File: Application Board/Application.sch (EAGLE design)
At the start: 53 parts, among them Q1 DMP2012SN-7, T1 FDN340P, T2 AP1117_LIN_REG, U1 LM3409HV'LM3409HV'

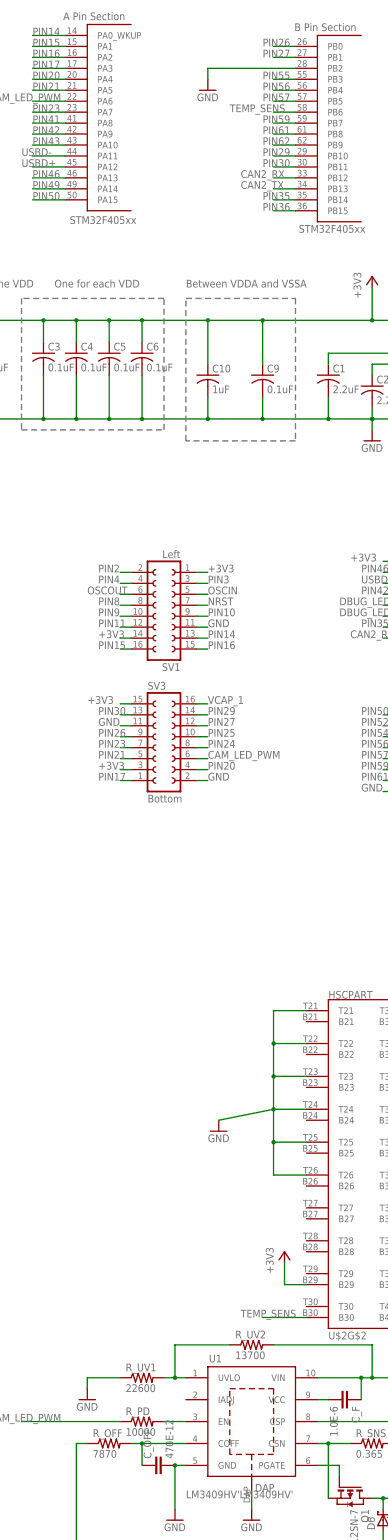
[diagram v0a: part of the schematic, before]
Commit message: Update 1/15/16 4:50pm
Added Temp_Sens Pullup Resistor, connected remaining air wires, modified
path of a few lines
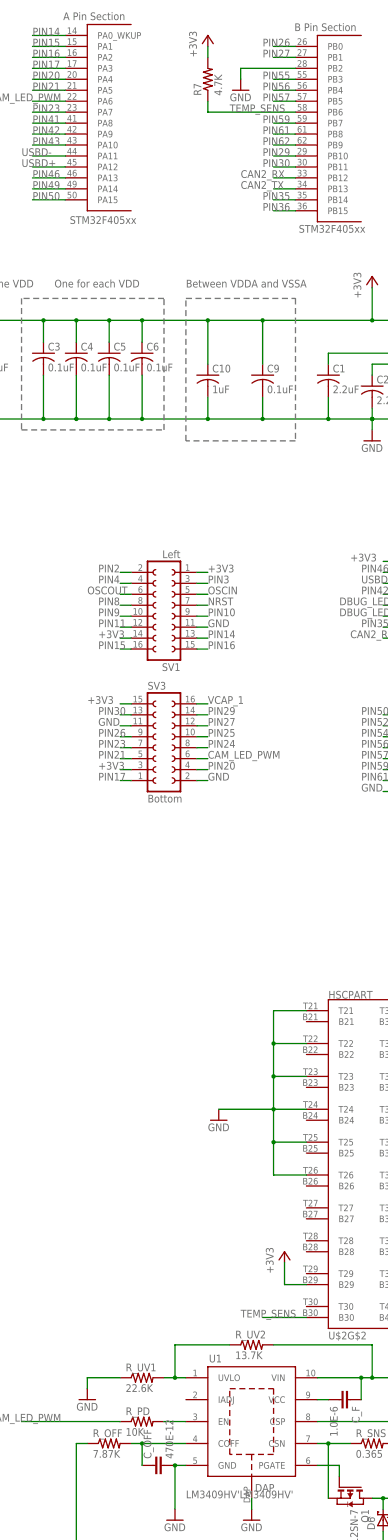
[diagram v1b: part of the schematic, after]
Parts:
- added R7: 4.7K, rcl:R-US_R0603
- R_OFF: value 7870 -> 7.87K
- R_PD: value 10000 -> 10K
- R_UV1: value 22600 -> 22.6K
- R_UV2: value 13700 -> 13.7K
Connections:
- net +3V3: now also R7.2
- net TEMP_SENS: now also R7.1
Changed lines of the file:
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@@
 <part name="+3V7" library="supply1" deviceset="+3V3" device=""/>
 <part name="GND11" library="supply1" deviceset="GND" device=""/>
-<part name="R_UV2" library="DiscreteComponents" deviceset="R-US_" device="R0603" value="13700"/>
-<part name="R_UV1" library="DiscreteComponents" deviceset="R-US_" device="R0603" value="22600"/>
-<part name="R_OFF" library="DiscreteComponents" deviceset="R-US_" device="R0603" value="7870"/>
+<part name="R_UV2" library="DiscreteComponents" deviceset="R-US_" device="R0603" value="13.7K"/>
+<part name="R_UV1" library="DiscreteComponents" deviceset="R-US_" device="R0603" value="22.6K"/>
+<part name="R_OFF" library="DiscreteComponents" deviceset="R-US_" device="R0603" value="7.87K"/>
 <part name="R_SNS" library="DiscreteComponents" deviceset="R-US_" device="R2512" value="0.365"/>
-<part name="R_PD" library="DiscreteComponents" deviceset="R-US_" device="R0603" value="10000"/>
+<part name="R_PD" library="DiscreteComponents" deviceset="R-US_" device="R0603" value="10K"/>
 <part name="L1" library="DiscreteComponents" deviceset="SRN8040" device="" value="15E-6"/>
 <part name="D6" library="DiscreteComponents" deviceset="SL12-E3/61T" device=""/>
@@
 <part name="P+5" library="supply1" deviceset="+12V" device=""/>
 <part name="GND18" library="supply1" deviceset="GND" device=""/>
+<part name="R7" library="rcl" deviceset="R-US_" device="R0603" value="4.7K"/>
+<part name="+3V5" library="supply1" deviceset="+3V3" device=""/>
 </parts>
 <sheets>
@@
 <instance part="+3V3" gate="G$1" x="198.12" y="71.12"/>
 <instance part="+3V4" gate="G$1" x="167.64" y="177.8"/>
-<instance part="GND3" gate="1" x="45.72" y="175.26"/>
+<instance part="GND3" gate="1" x="53.34" y="175.26"/>
 <instance part="FRAME2" gate="G$1" x="261.62" y="-15.24"/>
 <instance part="FRAME2" gate="G$2" x="431.8" y="-15.24"/>
@@
 <instance part="+3V8" gate="G$1" x="63.5" y="-93.98"/>
 <instance part="P+5" gate="1" x="121.92" y="-114.3"/>
-<instance part="GND18" gate="1" x="48.26" y="-66.04"/>
+<instance part="GND18" gate="1" x="48.26" y="-63.5"/>
+<instance part="R7" gate="G$1" x="45.72" y="177.8" rot="R90"/>
+<instance part="+3V5" gate="G$1" x="45.72" y="187.96"/>
 </instances>
 <busses>
@@
 <segment>
 <pinref part="U$1" gate="G$2" pin="PB2"/>
-<wire x1="66.04" y1="180.34" x2="45.72" y2="180.34" width="0.1524" layer="91"/>
-<wire x1="45.72" y1="180.34" x2="45.72" y2="177.8" width="0.1524" layer="91"/>
+<wire x1="66.04" y1="180.34" x2="53.34" y2="180.34" width="0.1524" layer="91"/>
+<wire x1="53.34" y1="180.34" x2="53.34" y2="177.8" width="0.1524" layer="91"/>
 <pinref part="GND3" gate="1" pin="GND"/>
 </segment>
@@
 <wire x1="68.58" y1="-45.72" x2="60.96" y2="-45.72" width="0.1524" layer="91"/>
 <junction x="60.96" y="-45.72"/>
-<wire x1="60.96" y1="-60.96" x2="48.26" y2="-63.5" width="0.1524" layer="91"/>
+<wire x1="60.96" y1="-60.96" x2="48.26" y2="-60.96" width="0.1524" layer="91"/>
 <junction x="60.96" y="-60.96"/>
 <pinref part="GND18" gate="1" pin="GND"/>
@@
 <wire x1="63.5" y1="-101.6" x2="68.58" y2="-101.6" width="0.1524" layer="91"/>
 </segment>
+<segment>
+<pinref part="R7" gate="G$1" pin="2"/>
+<pinref part="+3V5" gate="G$1" pin="+3V3"/>
+<wire x1="45.72" y1="185.42" x2="45.72" y2="182.88" width="0.1524" layer="91"/>
+</segment>
 </net>
 <net name="PIN14" class="0">
@@
 <segment>
 <pinref part="U$1" gate="G$2" pin="PB6"/>
-<wire x1="66.04" y1="170.18" x2="60.96" y2="170.18" width="0.1524" layer="91"/>
 <label x="50.8" y="170.18" size="1.778" layer="95"/>
-</segment>
-<segment>
+<wire x1="66.04" y1="170.18" x2="45.72" y2="170.18" width="0.1524" layer="91"/>
+<wire x1="45.72" y1="170.18" x2="45.72" y2="172.72" width="0.1524" layer="91"/>
+<pinref part="R7" gate="G$1" pin="1"/>
+</segment>
+<segment>

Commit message: Board Layout Finished！
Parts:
- C_F: value 1.0E-6 -> 1.0uF
- C_IN1, C_IN2: value 2.2E-6 -> 2.2uF
- C_OFF: value 470E-12 -> 470pF
- L1: value 15E-6 -> 15u
- S1: value SWITCH -> BOOT
- S2: value SWITCH -> RESET
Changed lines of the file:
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@@
 <?xml version="1.0" encoding="utf-8"?>
 <!DOCTYPE eagle SYSTEM "eagle.dtd">
-<eagle version="7.5.0">
+<eagle version="7.4.0">
 <drawing>
 <settings>
@@
 <part name="C11" library="rcl" deviceset="C-US" device="C0603" value="0.1uF"/>
 <part name="GND2" library="supply1" deviceset="GND" device=""/>
-<part name="S1" library="DiscreteComponents" deviceset="SWITCH" device=""/>
+<part name="S1" library="DiscreteComponents" deviceset="SWITCH" device="" value="BOOT"/>
 <part name="U$1" library="Other" deviceset="STM32F405" device=""/>
-<part name="S2" library="DiscreteComponents" deviceset="SWITCH" device=""/>
+<part name="S2" library="DiscreteComponents" deviceset="SWITCH" device="" value="RESET"/>
 <part name="R1" library="rcl" deviceset="R-US_" device="R0603" value="10K"/>
 <part name="R2" library="rcl" deviceset="R-US_" device="R0603" value="10K"/>
@@
 <part name="R_SNS" library="DiscreteComponents" deviceset="R-US_" device="R2512" value="0.365"/>
 <part name="R_PD" library="DiscreteComponents" deviceset="R-US_" device="R0603" value="10K"/>
-<part name="L1" library="DiscreteComponents" deviceset="SRN8040" device="" value="15E-6"/>
+<part name="L1" library="DiscreteComponents" deviceset="SRN8040" device="" value="15u"/>
 <part name="D6" library="DiscreteComponents" deviceset="SL12-E3/61T" device=""/>
 <part name="Q1" library="DiscreteComponents" deviceset="DMP2012SN-7" device=""/>
-<part name="C_F" library="eagle-ltspice" deviceset="C" device="C0603" value="1.0E-6"/>
-<part name="C_IN2" library="eagle-ltspice" deviceset="C" device="C0603" value="2.2E-6"/>
-<part name="C_IN1" library="eagle-ltspice" deviceset="C" device="C0603" value="2.2E-6"/>
-<part name="C_OFF" library="eagle-ltspice" deviceset="C" device="C0402" value="470E-12"/>
+<part name="C_F" library="eagle-ltspice" deviceset="C" device="C0603" value="1.0uF"/>
+<part name="C_IN2" library="eagle-ltspice" deviceset="C" device="C0603" value="2.2uF"/>
+<part name="C_IN1" library="eagle-ltspice" deviceset="C" device="C0603" value="2.2uF"/>
+<part name="C_OFF" library="eagle-ltspice" deviceset="C" device="C0402" value="470pF"/>
 <part name="GND12" library="supply1" deviceset="GND" device=""/>
 <part name="GND13" library="supply1" deviceset="GND" device=""/>
